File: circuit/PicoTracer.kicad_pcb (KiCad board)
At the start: 2 copper layers, 0 parts

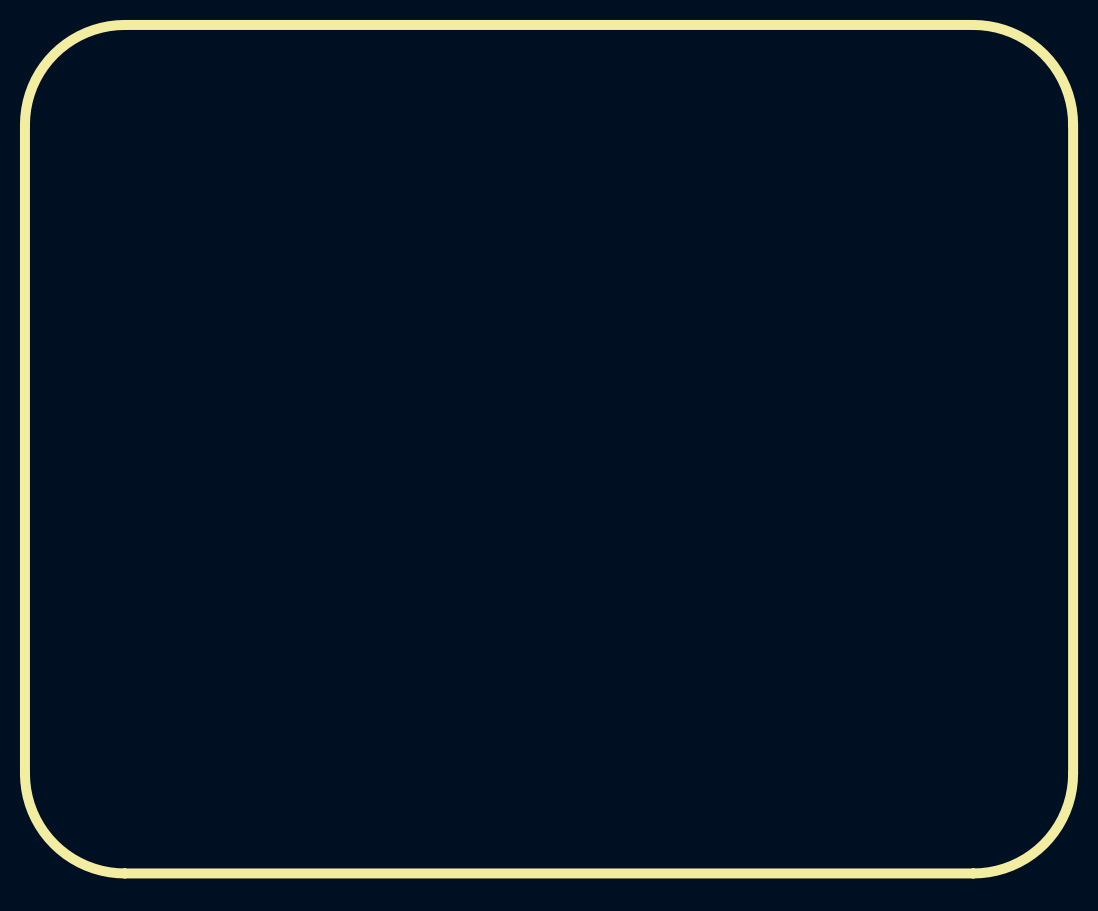
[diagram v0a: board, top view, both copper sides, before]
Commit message: 回路図：完成、配線図：配置のみ完了
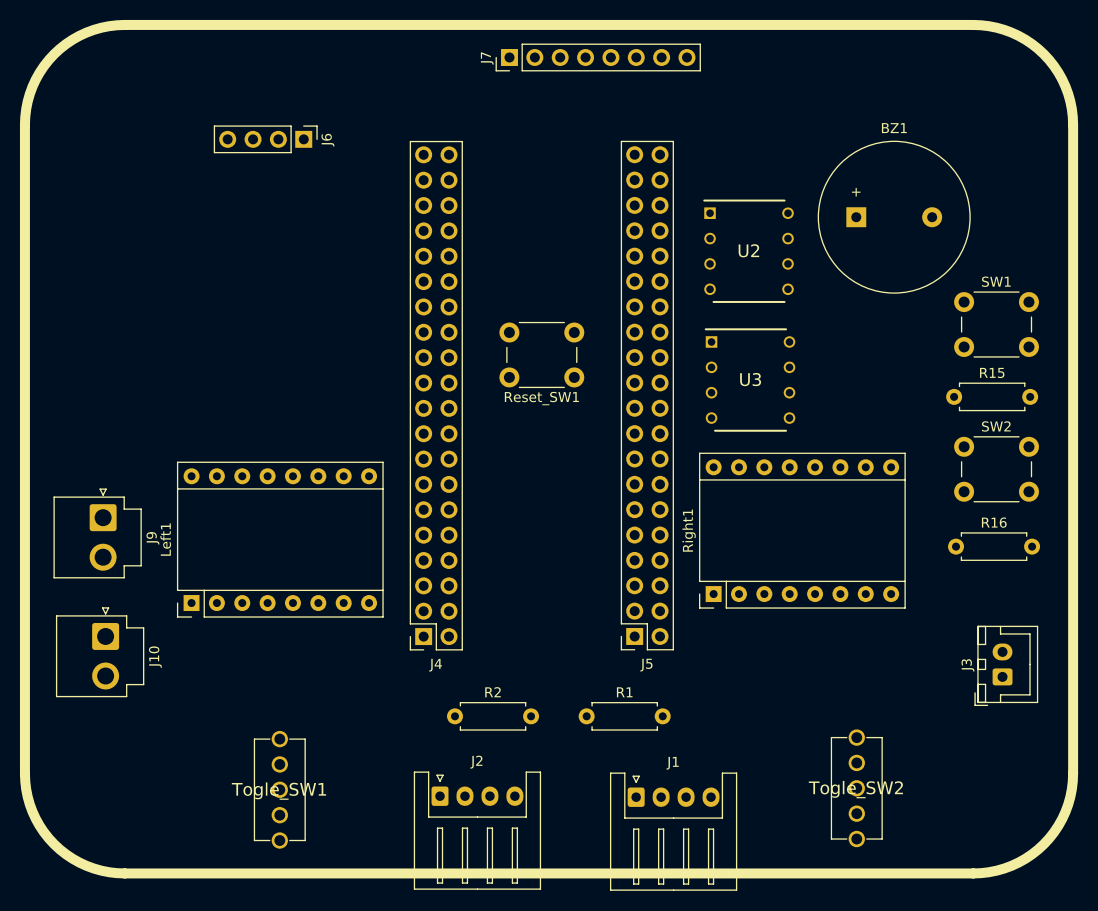
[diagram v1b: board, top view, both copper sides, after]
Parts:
- added BZ1: Buzzer, Buzzer_Beeper:Buzzer_15x7.5RM7.6, F.Cu at (182.2, 67.0)
- added J1: Conn_01x04_Socket, Connector_JST:JST_XH_S4B-XH-A_1x04_P2.50mm_Horizontal, F.Cu at (160.2, 125.1)
- added J10: Conn_01x02_Socket, Connector_JST:JST_VH_B2P-VH_1x02_P3.96mm_Vertical, F.Cu at (107.0, 109.0)
- added J2: Conn_01x04_Socket, Connector_JST:JST_XH_S4B-XH-A_1x04_P2.50mm_Horizontal, F.Cu at (140.5, 125.0)
- added J3: Conn_01x02_Socket, Connector_JST:JST_XH_B2B-XH-A_1x02_P2.50mm_Vertical, F.Cu at (196.8, 113.0)
- added J4: Conn_02x20_Top_Bottom, Connector_PinSocket_2.54mm:PinSocket_2x20_P2.54mm_Vertical_Raspipico, F.Cu at (138.9, 109.0)
- added J5: Conn_02x20_Top_Bottom, Connector_PinSocket_2.54mm:PinSocket_2x20_P2.54mm_Vertical_Raspipico, F.Cu at (160.0, 109.0)
- added J6: Conn_01x04_Socket, Connector_PinHeader_2.54mm:PinHeader_1x04_P2.54mm_Vertical, F.Cu at (126.8, 59.2)
- added J7: 8P8C, Connector_PinHeader_2.54mm:PinHeader_1x08_P2.54mm_Vertical, F.Cu at (147.5, 51.0)
- added J9: Conn_01x02_Socket, Connector_JST:JST_VH_B2P-VH_1x02_P3.96mm_Vertical, F.Cu at (106.8, 97.1)
- added Left1: Pololu_Breakout_A4988, Module:Pololu_Breakout-16_15.2x20.3mm, F.Cu at (115.6, 105.7)
- added R1: 5.1kΩ, Resistor_THT:R_Axial_DIN0207_L6.3mm_D2.5mm_P7.62mm_Horizontal, F.Cu at (155.2, 117.0)
- added R15: 5.1kΩ, Resistor_THT:R_Axial_DIN0207_L6.3mm_D2.5mm_P7.62mm_Horizontal, F.Cu at (192.0, 85.0)
- added R16: 5.1kΩ, Resistor_THT:R_Axial_DIN0207_L6.3mm_D2.5mm_P7.62mm_Horizontal, F.Cu at (192.2, 100.0)
- added R2: 1.0kΩ, Resistor_THT:R_Axial_DIN0207_L6.3mm_D2.5mm_P7.62mm_Horizontal, F.Cu at (142.0, 117.0)
- added Reset_SW1: SW_Push, Button_Switch_THT:SW_PUSH_6mm_H4.3mm, F.Cu at (153.9, 83.0)
- added Right1: Pololu_Breakout_A4988, Module:Pololu_Breakout-16_15.2x20.3mm, F.Cu at (167.9, 104.8)
- added SW1: SW_Push, Button_Switch_THT:SW_PUSH_6mm_H4.3mm, F.Cu at (193.0, 75.5)
- added SW2: SW_Push, Button_Switch_THT:SW_PUSH_6mm_H4.3mm, F.Cu at (193.0, 90.0)
- added Togle_SW1: SW_SPDT, SamacSys_Parts:2MS1T1B4VS2QES, F.Cu at (124.5, 121.8)
- added Togle_SW2: SW_SPDT, SamacSys_Parts:2MS1T1B4VS2QES, F.Cu at (182.2, 121.7)
- added U2: MCP3002, SamacSys_Parts:DIP781W56P254L950H533Q8N, F.Cu at (171.5, 70.4)
- added U3: MCP3002, SamacSys_Parts:DIP781W56P254L950H533Q8N, F.Cu at (171.6, 83.3)
